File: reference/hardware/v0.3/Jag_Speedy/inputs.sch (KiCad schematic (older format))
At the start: 51 parts, among them IC1 MPX4250AP, IC2 MPX4250AP, J6 Dual VR Conditioner

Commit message: Schematic pin mapping
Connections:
- net ADCClamp12 is gone; now on net ADCClamp10: C19.1, R31.2
- net ADCClamp13 is gone; now on net ADCClamp11: C20.1, R32.2
- net BRV-A4-3.3V is gone; now on net ADCClamp05: R33.2
- net Cam-CPU-D36 is gone; now on net ADCClamp02: C22.1, J6.7 (Pin_7)
- net 5V: no longer C1.2, C10.2, C11.2, C12.2, C13.2, C14.2, C15.2, C16.2, C17.2, C18.2, C19.2, C2.2, C20.2, C21.1, C22.2, C3.2, C4.1, C5.2, C6.2, C7.2, C8.1, C9.2, IC1.2 (GND), IC2.2 (GND), J6.6 (Pin_6), R28.2, R37.2, Z1.2
- net ADCClamp01: now also C21.2, J6.8 (Pin_8), R36.2; no longer C18.1, R30.2
- net ADCClamp02: now also R37.2; no longer C21.2, J6.8 (Pin_8), R36.2
- net ADCClamp03: now also C5.1, R18.2; no longer C11.1, R22.2
- net ADCClamp04: now also C11.1, R22.2; no longer C16.1, R27.2, R28.1, R33.1
- net ADCClamp05: no longer C5.1, R18.2
- net ADCClamp06: now also C4.2, R17.2; no longer C17.1, R29.2
- net ADCClamp07: now also C8.2, R21.2; no longer C4.2, R17.2
- net ADCClamp08: now also C17.1, R29.2; no longer C8.2, R21.2
- net ADCClamp10: no longer C2.1, R19.1
- net ADCClamp11: no longer R20.2, Z1.1
- new net: C16.1, R27.2, R28.1, R33.1
- new net ADCClamp09: C18.1, R30.2
- new net ClutchIn-Signal: R20.2, Z1.1
- new net FlexFuel-Signal: C2.1, R19.1
- new net SensorGnd: C1.2, C10.2, C11.2, C12.2, C13.2, C14.2, C15.2, C16.2, C17.2, C18.2, C19.2, C2.2, C20.2, C21.1, C22.2, C3.2, C4.1, C5.2, C6.2, C7.2, C8.1, C9.2, IC1.2 (GND), IC2.2 (GND), J6.6 (Pin_6), R28.2, Z1.2
- no-connect marks 7 -> 6
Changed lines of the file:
@@
 Text GLabel 1050 1250 0    50   Input ~ 0
 O2Sensor
-Text GLabel 1900 1150 1    50   Input ~ 0
-ADCClamp05
 $Comp
 L Device:C C1
@@
 	1    0    0    -1
 $EndComp
-Text GLabel 2350 1250 2    50   Input ~ 0
-O2-A8-5V
+Text GLabel 2350 1250 2    50   Output ~ 0
+O2-Signal-5V
 Wire Wire Line
 	1050 1250 1250 1250
@@
 Connection ~ 1250 1250
 Wire Wire Line
-	1800 1250 1900 1250
-Wire Wire Line
 	2000 1250 2350 1250
 Connection ~ 2000 1250
-Wire Wire Line
-	1900 1150 1900 1250
-Connection ~ 1900 1250
-Wire Wire Line
-	1900 1250 2000 1250
 Wire Wire Line
 	2000 1550 1650 1550
@@
 Text GLabel 3700 1250 0    50   Input ~ 0
 TPSSensor
-Text GLabel 4550 1150 1    50   Input ~ 0
-ADCClamp03
 $Comp
 L Device:C C9
@@
 	1    0    0    -1
 $EndComp
-Text GLabel 5000 1250 2    50   Input ~ 0
-TPS-A2-5V
+Text GLabel 5000 1250 2    50   Output ~ 0
+TPS-Signal-5V
 Wire Wire Line
 	3700 1250 3900 1250
@@
 Connection ~ 3900 1250
 Wire Wire Line
-	4450 1250 4550 1250
-Wire Wire Line
 	4650 1250 5000 1250
 Connection ~ 4650 1250
-Wire Wire Line
-	4550 1150 4550 1250
-Connection ~ 4550 1250
-Wire Wire Line
-	4550 1250 4650 1250
 Wire Wire Line
 	4650 1550 4300 1550
@@
 	1    0    0    -1
 $EndComp
-Text GLabel 1150 2850 1    50   Input ~ 0
-MAP-A3-5V
+Text GLabel 1150 2850 1    50   Output ~ 0
+MAP-Signal-5V
 Wire Wire Line
 	2150 3150 2150 3300
@@
 Connection ~ 2150 3600
 Connection ~ 1750 3600
-Wire Wire Line
-	1150 2850 1150 2950
 Wire Wire Line
 	1150 3900 1550 3900
@@
 	1    0    0    -1
 $EndComp
-Text GLabel 2900 2850 1    50   Input ~ 0
-Barro-A5-5V
+Text GLabel 2900 2850 1    50   Output ~ 0
+Barro-Signal-5V
 Wire Wire Line
 	3900 3150 3900 3300
@@
 Connection ~ 3500 3600
 Wire Wire Line
-	2900 2850 2900 2900
-Wire Wire Line
 	2900 3900 3300 3900
 Wire Wire Line
@@
 Text Notes 2650 4200 0    118  ~ 0
 Barro Sensor
-Text GLabel 6600 1250 2    50   Input ~ 0
-BRV-A4-3.3V
+Text GLabel 6600 1250 2    50   Output ~ 0
+BRV-Signal-5V
 $Comp
 L Device:R R33
@@
 Text GLabel 6600 1550 2    50   Input ~ 0
 SensorGnd
-Text GLabel 6600 950  2    50   Input ~ 0
-ADCClamp04
 Wire Wire Line
 	6150 1250 6050 1250
@@
 Connection ~ 6050 1550
 Wire Wire Line
-	6600 1250 6450 1250
-Wire Wire Line
-	6050 950  6050 1250
+	6600 1250 6500 1250
 Text Notes 5350 750  0    118  ~ 0
 Battery Reference Voltage
-Wire Wire Line
-	6050 950  6600 950
 Text GLabel 6600 850  2    50   Input ~ 0
 12V
 Wire Wire Line
 	6600 850  5750 850
-Text GLabel 6650 2250 2    50   Input ~ 0
-IAT-A0-5V
+Text GLabel 6650 2250 2    50   Output ~ 0
+IAT-Signal-5V
 Text GLabel 6650 1850 2    50   Input ~ 0
 5V
-Text GLabel 6650 1950 2    50   Input ~ 0
-ADCClamp06
 Text GLabel 6650 2550 2    50   Input ~ 0
 SensorGnd
@@
 Wire Wire Line
 	6450 2250 6300 2250
-Wire Wire Line
-	6650 2250 6550 2250
 Connection ~ 6450 2250
 Wire Wire Line
@@
 	6450 2550 5700 2550
 Connection ~ 6450 2550
-Wire Wire Line
-	6650 1950 6550 1950
-Wire Wire Line
-	6550 1950 6550 2250
-Connection ~ 6550 2250
-Wire Wire Line
-	6550 2250 6450 2250
 Text Notes 4900 2150 0    118  ~ 0
 Inlet Air\nTemp\nSensor
-Text GLabel 6650 3400 2    50   Input ~ 0
-CLT-A1-5V
+Text GLabel 6650 3400 2    50   Output ~ 0
+CLT-Signal-5V
 Text GLabel 6650 3000 2    50   Input ~ 0
 5V
-Text GLabel 6650 3100 2    50   Input ~ 0
-ADCClamp01
 Text GLabel 6650 3700 2    50   Input ~ 0
 SensorGnd
@@
 Wire Wire Line
 	6450 3400 6300 3400
-Wire Wire Line
-	6650 3400 6550 3400
 Connection ~ 6450 3400
 Wire Wire Line
@@
 	6450 3700 5700 3700
 Connection ~ 6450 3700
-Wire Wire Line
-	6650 3100 6550 3100
-Wire Wire Line
-	6550 3100 6550 3400
-Connection ~ 6550 3400
-Wire Wire Line
-	6550 3400 6450 3400
 Text Notes 4900 3300 0    118  ~ 0
 Coolant\nTemp\nSensor
@@
 Cam-CPU-D36
 Text GLabel 9800 1700 1    50   Input ~ 0
-ADCClamp02
+ADCClamp01
 $Comp
 L Device:C C22
@@
 	9250 2600 9150 2600
 Wire Wire Line
-	9750 2600 9800 2600
-Wire Wire Line
 	9750 2300 9800 2300
 Wire Wire Line
@@
 Wire Wire Line
 	8700 2700 8700 2500
-Text GLabel 1000 2850 1    50   Input ~ 0
-ADCClamp07
-Text GLabel 2750 2800 1    50   Input ~ 0
-ADCClamp08
-Wire Wire Line
-	2750 2800 2750 2900
-Wire Wire Line
-	2750 2900 2900 2900
-Connection ~ 2900 2900
-Wire Wire Line
-	2900 2900 2900 3900
-Wire Wire Line
-	1000 2850 1000 2950
-Wire Wire Line
-	1000 2950 1150 2950
-Connection ~ 1150 2950
-Wire Wire Line
-	1150 2950 1150 3900
-Wire Wire Line
-	9750 2400 9950 2400
+Wire Wire Line
+	9750 2400 9800 2400
 Wire Wire Line
 	9750 2500 10350 2500
@@
 	8050 2450 8050 2550
 Text GLabel 9800 3200 3    50   Input ~ 0
-ADCClamp09
+ADCClamp02
 $Comp
 L Device:R R37
@@
 Wire Wire Line
 	8700 3200 9100 3200
-Wire Wire Line
-	9400 3200 9800 3200
-Wire Wire Line
-	9800 3200 9800 2600
-Connection ~ 9800 2600
-Wire Wire Line
-	9800 2600 10350 2600
 Text GLabel 9950 3200 3    50   Input ~ 0
 SensorGnd
 Wire Wire Line
 	9950 3200 9950 3100
-Wire Wire Line
-	9950 3200 9800 3200
-Connection ~ 9800 3200
 Wire Wire Line
 	9950 2800 9950 2400
@@
 Text Notes 900  4850 0    118  ~ 0
 Flex Sensor
-Text GLabel 1250 5250 0    50   Input ~ 0
-ADCClamp10
 Text GLabel 1250 5450 0    50   Input ~ 0
 FlexFuelSensor
-Text GLabel 1250 5050 0    50   Input ~ 0
-FlexFuel
+Text GLabel 1250 5050 0    50   Output ~ 0
+FlexFuel-Signal
 $Comp
 L Device:R R19
@@
 Wire Wire Line
 	1350 5050 1250 5050
-Wire Wire Line
-	1250 5250 1350 5250
 Connection ~ 1350 5250
 Wire Wire Line
@@
 Wire Wire Line
 	1500 5250 1550 5250
-Text GLabel 3650 5000 2    50   Input ~ 0
-ADCClamp11
 Text Notes 2950 4800 0    118  ~ 0
 Clutch Input
 Text GLabel 2950 5250 0    50   Input ~ 0
 ClutchSwitch
-Text GLabel 3650 5250 2    50   Input ~ 0
-ClutchIn-CPU-D51
+Text GLabel 3650 5250 2    50   Output ~ 0
+ClutchIn-Signal
 Text GLabel 3400 6000 3    50   Input ~ 0
 SensorGnd
@@
 Connection ~ 3400 5250
 Wire Wire Line
-	3650 5000 3400 5000
-Wire Wire Line
-	3400 5000 3400 5250
-Wire Wire Line
 	3400 6000 3400 5850
 NoConn ~ 3800 3100
@@
 Text GLabel 6650 4150 2    50   Input ~ 0
 5V
-Text GLabel 6650 4250 2    50   Input ~ 0
-ADCClamp12
 Text GLabel 6650 4850 2    50   Input ~ 0
 SensorGnd
@@
 Wire Wire Line
 	6450 4550 6300 4550
-Wire Wire Line
-	6650 4550 6550 4550
 Connection ~ 6450 4550
 Wire Wire Line
@@
 	6450 4850 5700 4850
 Connection ~ 6450 4850
-Wire Wire Line
-	6650 4250 6550 4250
-Wire Wire Line
-	6550 4250 6550 4550
-Connection ~ 6550 4550
-Wire Wire Line
-	6550 4550 6450 4550
 Text Notes 4750 4450 0    118  ~ 0
 Fuel\nPressure\nSensor
 Text GLabel 6650 4550 2    50   Output ~ 0
-FPress-A10-5V
+FPress-Signal-5V
 Text GLabel 6650 5400 2    50   Input ~ 0
 5V
-Text GLabel 6650 5500 2    50   Input ~ 0
-ADCClamp13
 Text GLabel 6650 6100 2    50   Input ~ 0
 SensorGnd
@@
 Wire Wire Line
 	6450 5800 6300 5800
-Wire Wire Line
-	6650 5800 6550 5800
 Connection ~ 6450 5800
 Wire Wire Line
@@
 	6450 6100 5700 6100
 Connection ~ 6450 6100
-Wire Wire Line
-	6650 5500 6550 5500
-Wire Wire Line
-	6550 5500 6550 5800
-Connection ~ 6550 5800
-Wire Wire Line
-	6550 5800 6450 5800
 Text Notes 4750 5700 0    118  ~ 0
 Oil\nPressure\nSensor
 Text GLabel 6650 5800 2    50   Output ~ 0
-OPress-A11-5V
+OPress-Signal-5V
 Text GLabel 1650 3100 3    50   Input ~ 0
 SensorGnd
 Text GLabel 3400 3100 3    50   Input ~ 0
 SensorGnd
-Text GLabel 2550 6950 2    50   Input ~ 0
-ADCClamp14
-NoConn ~ 2550 6950
 $Comp
 L MPX4250AP:MPX4250AP IC1
@@
 	0    -1   -1   0
 $EndComp
+Wire Wire Line
+	1800 1250 2000 1250
+Wire Wire Line
+	4450 1250 4650 1250
+Wire Wire Line
+	6450 2250 6650 2250
+Wire Wire Line
+	6450 3400 6650 3400
+Wire Wire Line
+	2900 2850 2900 3900
+Wire Wire Line
+	1150 2850 1150 3900
+Wire Wire Line
+	6450 5800 6650 5800
+Wire Wire Line
+	6450 4550 6650 4550
+Wire Wire Line
+	9750 2600 10350 2600
+Wire Wire Line
+	9400 3200 9800 3200
+Wire Wire Line
+	9800 3200 9800 2400
+Connection ~ 9800 2400
+Wire Wire Line
+	9800 2400 9950 2400
+Text GLabel 2350 1150 2    50   Input ~ 0
+ADCClamp03
+Wire Wire Line
+	2350 1150 2000 1150
+Wire Wire Line
+	2000 1150 2000 1250
+Text GLabel 5000 1150 2    50   Input ~ 0
+ADCClamp04
+Wire Wire Line
+	5000 1150 4650 1150
+Wire Wire Line
+	4650 1150 4650 1250
+Text GLabel 6600 1150 2    50   Input ~ 0
+ADCClamp05
+Wire Wire Line
+	6600 1150 6500 1150
+Wire Wire Line
+	6500 1150 6500 1250
+Connection ~ 6500 1250
+Wire Wire Line
+	6500 1250 6450 1250
+Text GLabel 1050 2850 1    50   Input ~ 0
+ADCClamp06
+Wire Wire Line
+	1050 2850 1050 3900
+Wire Wire Line
+	1050 3900 1150 3900
+Connection ~ 1150 3900
+Text GLabel 2800 2850 1    50   Input ~ 0
+ADCClamp07
+Wire Wire Line
+	2800 2850 2800 3900
+Wire Wire Line
+	2800 3900 2900 3900
+Connection ~ 2900 3900
+Text GLabel 6650 2150 2    50   Input ~ 0
+ADCClamp08
+Wire Wire Line
+	6650 2150 6450 2150
+Wire Wire Line
+	6450 2150 6450 2250
+Text GLabel 6650 3300 2    50   Input ~ 0
+ADCClamp09
+Wire Wire Line
+	6650 3300 6450 3300
+Wire Wire Line
+	6450 3300 6450 3400
+Text GLabel 6650 4450 2    50   Input ~ 0
+ADCClamp10
+Wire Wire Line
+	6650 4450 6450 4450
+Wire Wire Line
+	6450 4450 6450 4550
+Text GLabel 6650 5700 2    50   Input ~ 0
+ADCClamp11
+Wire Wire Line
+	6650 5700 6450 5700
+Wire Wire Line
+	6450 5700 6450 5800
 $EndSCHEMATC

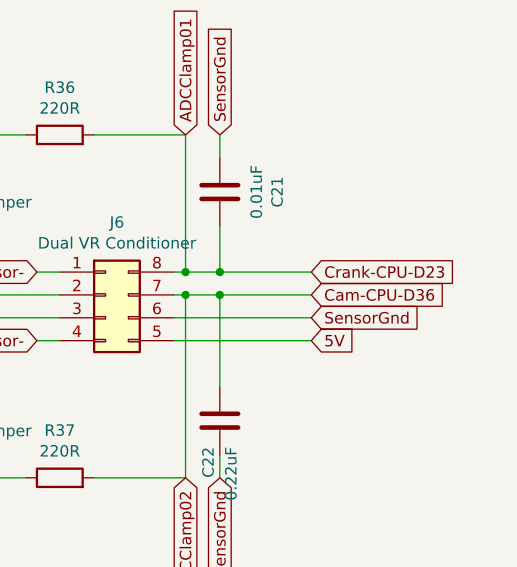
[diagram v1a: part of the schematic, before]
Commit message: Canbus Tranceiver
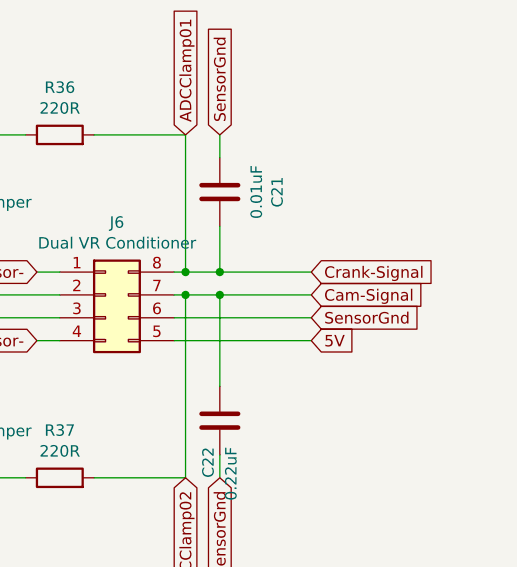
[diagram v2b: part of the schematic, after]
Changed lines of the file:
@@
 CamSensor+
 Text GLabel 10350 2300 2    50   Input ~ 0
-Crank-CPU-D23
+Crank-Signal
 Text GLabel 10350 2400 2    50   Input ~ 0
-Cam-CPU-D36
+Cam-Signal
 Text GLabel 9800 1700 1    50   Input ~ 0
 ADCClamp01

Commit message: MOSFET Drivers
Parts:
- IC1, IC2: symbol MPX4250AP:MPX4250AP -> Jag_Speedy-rescue:MPX4250AP-MPX4250AP
- Z1: symbol MM3Z5V1ST1G:MM3Z5V1ST1G -> Jag_Speedy-rescue:MM3Z5V1ST1G-MM3Z5V1ST1G
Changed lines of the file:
@@
 $EndComp
 $Comp
-L MM3Z5V1ST1G:MM3Z5V1ST1G Z1
+L Jag_Speedy-rescue:MM3Z5V1ST1G-MM3Z5V1ST1G Z1
 U 1 1 5F17D884
 P 3400 5250
@@
 SensorGnd
 $Comp
-L MPX4250AP:MPX4250AP IC1
+L Jag_Speedy-rescue:MPX4250AP-MPX4250AP IC1
 U 1 1 5F4B3E38
 P 1550 3100
@@
 $EndComp
 $Comp
-L MPX4250AP:MPX4250AP IC2
+L Jag_Speedy-rescue:MPX4250AP-MPX4250AP IC2
 U 1 1 5F4B556C
 P 3300 3100

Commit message: Rationalise level shifting
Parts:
- IC1, IC2: symbol Jag_Speedy-rescue:MPX4250AP-MPX4250AP -> Jag_Speedy-rescue:MPX4250AP-MPX4250AP-Jag_Speedy-rescue
- Z1: symbol Jag_Speedy-rescue:MM3Z5V1ST1G-MM3Z5V1ST1G -> Jag_Speedy-rescue:MM3Z5V1ST1G-MM3Z5V1ST1G-Jag_Speedy-rescue
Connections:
- net 5V: no longer R23.1, R24.1, R25.1, R26.1
- new net 3V3: R23.1, R24.1, R25.1, R26.1
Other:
- moved on the sheet: C1, C10, C11, C2, C3, C4, C5, C6, C7, C8, C9, IC1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

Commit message: SMD Update
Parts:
- C1, C10, C11, C12, C13, C14, C15, C16, C17, C18, C19, C2, C20, C21, C22, C3, C4, C5, C6, C7, C8, C9: footprint Capacitor_THT:CP_Radial_D5.0mm_P2.50mm -> Capacitor_SMD:C_0805_2012Metric
- IC1, IC2: footprint Connector_PinHeader_2.54mm:PinHeader_1x06_P2.54mm_Vertical -> Connector_PinHeader_2.54mm:PinHeader_1x05_P2.54mm_Vertical
- R17, R18, R19, R20, R21, R22, R23, R24, R25, R26, R27, R28, R29, R30, R31, R32, R33, R34, R35, R36, R37: footprint Resistor_THT:R_Axial_DIN0207_L6.3mm_D2.5mm_P2.54mm_Vertical -> Resistor_SMD:R_0805_2012Metric
- Z1: footprint Diode_THT:D_DO-35_SOD27_P10.16mm_Horizontal -> Diode_SMD:D_SOD-323

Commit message: VR Conditioner
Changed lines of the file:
@@
 	1    0    0    -1
 $EndComp
-Text GLabel 1150 4150 1    50   Output ~ 0
+Text GLabel 1350 4200 1    50   Output ~ 0
 MAP-Signal-5V
 Wire Wire Line
@@
 Connection ~ 1750 4900
 Wire Wire Line
-	1150 5200 1550 5200
-Wire Wire Line
 	1550 4750 1550 5200
-Connection ~ 1550 5200
 Wire Wire Line
 	1550 5200 1750 5200
@@
 	1    0    0    -1
 $EndComp
-Text GLabel 2900 4150 1    50   Output ~ 0
+Text GLabel 3100 4200 1    50   Output ~ 0
 Barro-Signal-5V
 Wire Wire Line
@@
 Connection ~ 3500 4900
 Wire Wire Line
-	2900 5200 3300 5200
-Wire Wire Line
 	3300 4750 3300 5200
-Connection ~ 3300 5200
 Wire Wire Line
 	3300 5200 3500 5200
@@
 Text GLabel 6650 5800 2    50   Output ~ 0
 OPress-Signal-3V3
-Text GLabel 1650 4400 3    50   Input ~ 0
-SensorGnd
-Text GLabel 3400 4400 3    50   Input ~ 0
-SensorGnd
 $Comp
 L Jag_Speedy-rescue:MPX4250AP-MPX4250AP-Jag_Speedy-rescue IC1
@@
 	6450 3400 6650 3400
 Wire Wire Line
-	2900 4150 2900 5200
-Wire Wire Line
-	1150 4150 1150 5200
-Wire Wire Line
 	6450 5800 6650 5800
 Wire Wire Line
@@
 Wire Wire Line
 	6500 1250 6450 1250
-Text GLabel 1050 4150 1    50   Input ~ 0
+Text GLabel 1250 4200 1    50   Input ~ 0
 ADCClamp06
-Wire Wire Line
-	1050 4150 1050 5200
-Wire Wire Line
-	1050 5200 1150 5200
-Connection ~ 1150 5200
-Text GLabel 2800 4150 1    50   Input ~ 0
+Text GLabel 3000 4200 1    50   Input ~ 0
 ADCClamp07
-Wire Wire Line
-	2800 4150 2800 5200
-Wire Wire Line
-	2800 5200 2900 5200
-Connection ~ 2900 5200
 Text GLabel 6650 2150 2    50   Input ~ 0
 ADCClamp08
@@
 Wire Wire Line
 	6450 5700 6450 5800
+Wire Wire Line
+	1650 4400 1650 4900
+Wire Wire Line
+	1650 4900 1750 4900
+Wire Wire Line
+	3400 4400 3400 4900
+Wire Wire Line
+	3400 4900 3500 4900
+Wire Wire Line
+	1550 5200 1350 5200
+Wire Wire Line
+	1250 5200 1250 4200
+Connection ~ 1550 5200
+Wire Wire Line
+	1350 4200 1350 5200
+Connection ~ 1350 5200
+Wire Wire Line
+	1350 5200 1250 5200
+Wire Wire Line
+	3000 4200 3000 5200
+Wire Wire Line
+	3000 5200 3100 5200
+Connection ~ 3300 5200
+Wire Wire Line
+	3100 4200 3100 5200
+Connection ~ 3100 5200
+Wire Wire Line
+	3100 5200 3300 5200
 $EndSCHEMATC
